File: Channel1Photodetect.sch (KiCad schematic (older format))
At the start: 10 parts

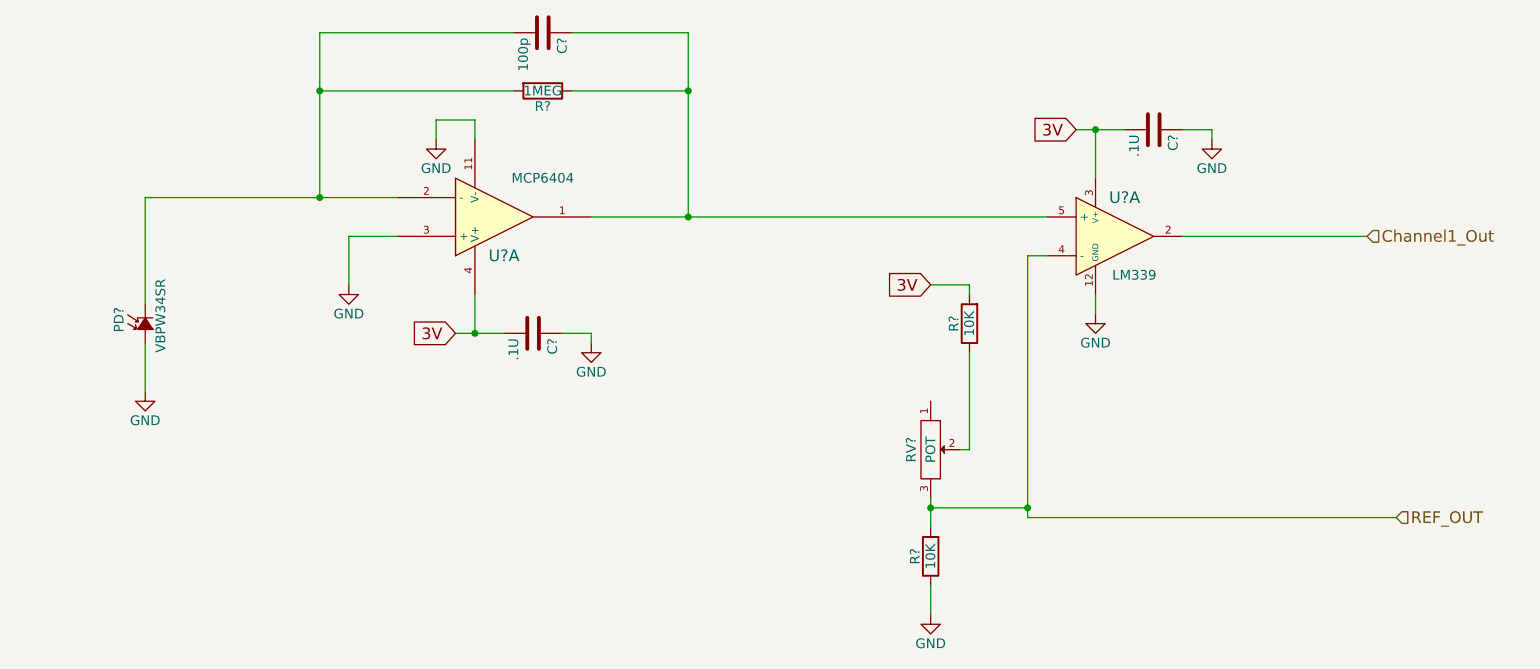
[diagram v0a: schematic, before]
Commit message: Added power regulator, VGND and test points
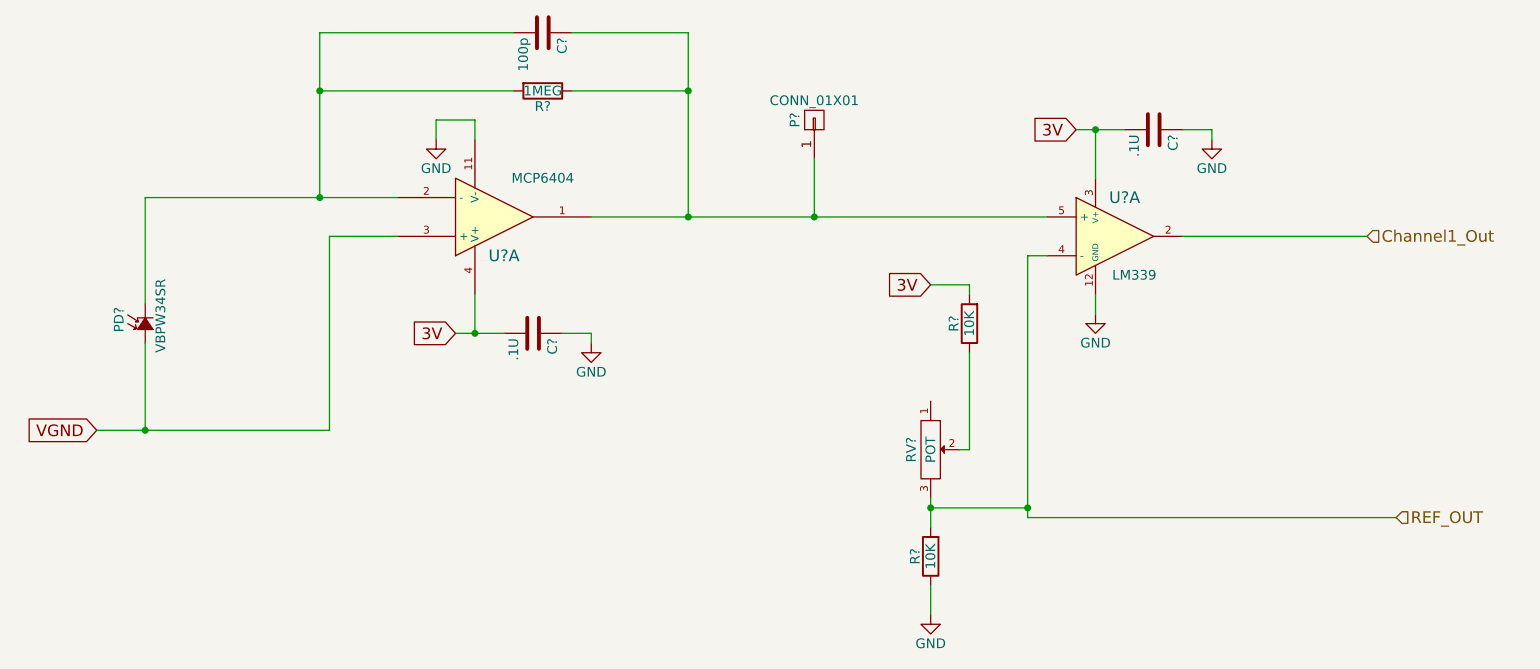
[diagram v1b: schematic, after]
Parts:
- added P?: CONN_01X01, symbol CONN_01X01
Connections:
- net GND: no longer PD?.1 (A), U?.3 (+)
- net at C?.1, R?.1, U?.1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: now also P?.1 (P1)
- new net VGND: PD?.1 (A), U?.3 (+)
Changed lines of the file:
@@
 LIBS:memory
 LIBS:xilinx
-LIBS:special
 LIBS:microcontrollers
 LIBS:dsp
@@
 Wire Wire Line
 	4200 2850 4200 2950
-$Comp
-L GND #PWR?
-U 1 1 5552D532
-P 3750 3700
-F 0 "#PWR?" H 3750 3450 50  0001 C CNN
-F 1 "GND" H 3750 3550 50  0000 C CNN
-F 2 "" H 3750 3700 60  0000 C CNN
-F 3 "" H 3750 3700 60  0000 C CNN
-	1    3750 3700
-	1    0    0    -1
-$EndComp
-Wire Wire Line
-	4000 3450 3750 3450
-Wire Wire Line
-	3750 3450 3750 3700
+Wire Wire Line
+	3650 3450 4000 3450
 Text GLabel 4300 3950 0    60   Input ~ 0
 3V
@@
 Wire Wire Line
 	5000 3950 5000 4000
-$Comp
-L GND #PWR?
-U 1 1 5552D54D
-P 2700 4250
-F 0 "#PWR?" H 2700 4000 50  0001 C CNN
-F 1 "GND" H 2700 4100 50  0000 C CNN
-F 2 "" H 2700 4250 60  0000 C CNN
-F 3 "" H 2700 4250 60  0000 C CNN
-	1    2700 4250
-	1    0    0    -1
-$EndComp
-Wire Wire Line
-	2700 4000 2700 4250
 $Comp
 L LM339 U?
@@
 	7250 4900 9150 4900
 Connection ~ 7250 4850
+$Comp
+L CONN_01X01 P?
+U 1 1 55569411
+P 6150 2850
+F 0 "P?" H 6150 2950 50  0000 C CNN
+F 1 "CONN_01X01" V 6250 2850 50  0000 C CNN
+F 2 "" H 6150 2850 60  0000 C CNN
+F 3 "" H 6150 2850 60  0000 C CNN
+	1    6150 2850
+	0    -1   -1   0
+$EndComp
+Wire Wire Line
+	6150 3050 6150 3350
+Connection ~ 6150 3350
+Wire Wire Line
+	3650 4450 3650 3450
+Wire Wire Line
+	2450 4450 3650 4450
+Wire Wire Line
+	2700 4450 2700 4000
+Text GLabel 2450 4450 0    60   Input ~ 0
+VGND
+Connection ~ 2700 4450
 $EndSCHEMATC

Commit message: Added libraries and imported components into the layout
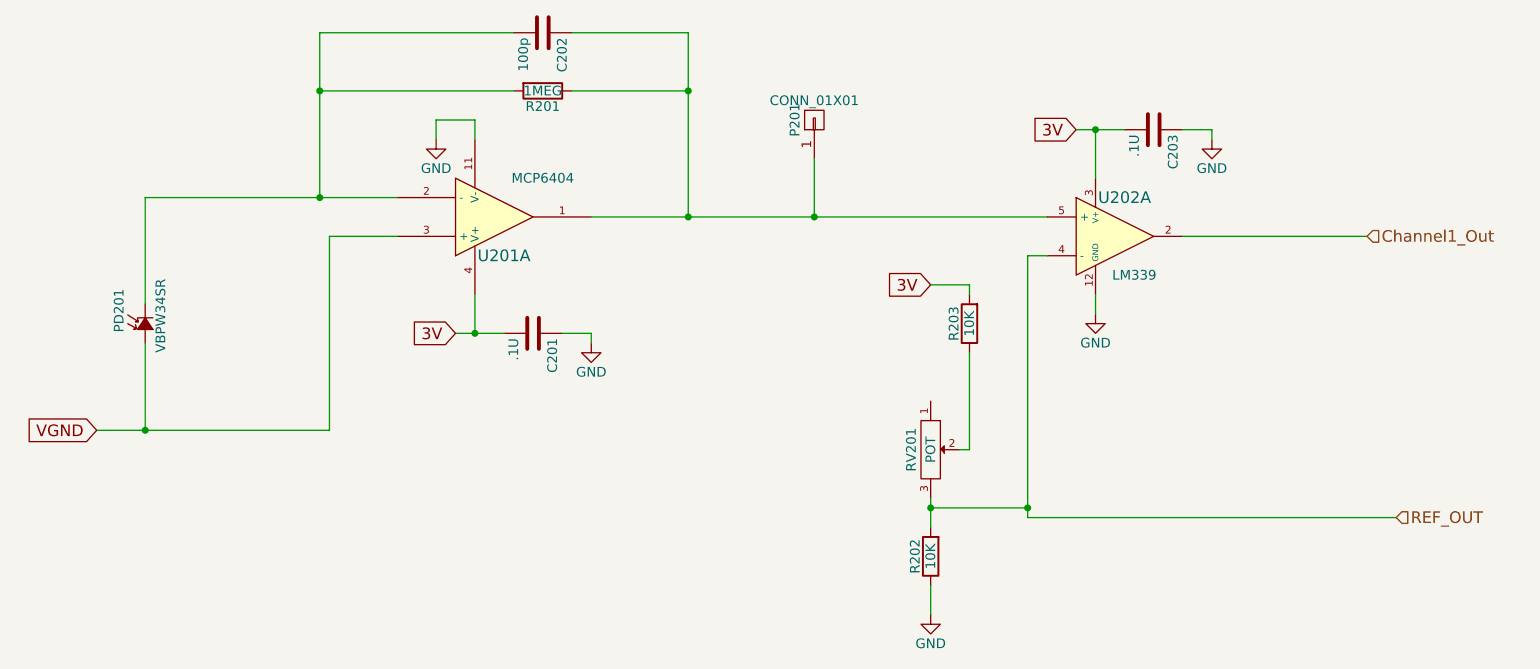
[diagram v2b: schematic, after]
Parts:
- gave numbers to parts that had none: 11
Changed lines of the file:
@@
 $EndDescr
 $Comp
-L R R?
+L R R201
 U 1 1 5552D4FD
 P 4750 2700
-F 0 "R?" V 4830 2700 50  0000 C CNN
+F 0 "R201" V 4830 2700 50  0000 C CNN
 F 1 "1MEG" V 4750 2700 50  0000 C CNN
 F 2 "" V 4680 2700 30  0000 C CNN
@@
 $EndComp
 $Comp
-L C C?
+L C C202
 U 1 1 5552D504
 P 4750 2400
-F 0 "C?" H 4775 2500 50  0000 L CNN
+F 0 "C202" H 4775 2500 50  0000 L CNN
 F 1 "100p" H 4775 2300 50  0000 L CNN
 F 2 "" H 4788 2250 30  0000 C CNN
@@
 $EndComp
 $Comp
-L MCP6404-E/SL U?
+L MCP6404-E/SL U201
 U 1 1 5552D50D
 P 4500 3350
-F 0 "U?" H 4550 3550 60  0000 C CNN
+F 0 "U201" H 4550 3550 60  0000 C CNN
 F 1 "MCP6404" H 4750 3150 50  0000 C CNN
 F 2 "" H 4500 3350 60  0000 C CNN
@@
 $EndComp
 $Comp
-L Photodiode PD?
+L Photodiode PD201
 U 1 1 5552D516
 P 2700 3900
-F 0 "PD?" H 2655 4035 50  0000 L CNN
+F 0 "PD201" H 2655 4035 50  0000 L CNN
 F 1 "VBPW34SR" H 2550 3820 50  0000 L CNN
 F 2 "" V 2700 3900 60  0000 C CNN
@@
 Connection ~ 5500 2700
 $Comp
-L GND #PWR?
+L GND #PWR05
 U 1 1 5552D529
 P 4200 2950
-F 0 "#PWR?" H 4200 2700 50  0001 C CNN
+F 0 "#PWR05" H 4200 2700 50  0001 C CNN
 F 1 "GND" H 4200 2800 50  0000 C CNN
 F 2 "" H 4200 2950 60  0000 C CNN
@@
 	4400 3950 4400 3750
 $Comp
-L C C?
+L C C201
 U 1 1 5552D53D
 P 4700 3950
-F 0 "C?" H 4725 4050 50  0000 L CNN
+F 0 "C201" H 4725 4050 50  0000 L CNN
 F 1 ".1U" H 4725 3850 50  0000 L CNN
 F 2 "" H 4738 3800 30  0000 C CNN
@@
 $EndComp
 $Comp
-L GND #PWR?
+L GND #PWR06
 U 1 1 5552D544
 P 5000 4000
-F 0 "#PWR?" H 5000 3750 50  0001 C CNN
+F 0 "#PWR06" H 5000 3750 50  0001 C CNN
 F 1 "GND" H 5000 3850 50  0000 C CNN
 F 2 "" H 5000 4000 60  0000 C CNN
@@
 	5000 3950 5000 4000
 $Comp
-L LM339 U?
+L LM339 U202
 U 1 1 5552D556
 P 7700 3450
-F 0 "U?" H 7750 3650 60  0000 C CNN
+F 0 "U202" H 7750 3650 60  0000 C CNN
 F 1 "LM339" H 7800 3250 50  0000 C CNN
 F 2 "" H 7700 3450 60  0000 C CNN
@@
 3V
 $Comp
-L R R?
+L R R203
 U 1 1 5552D55F
 P 6950 3900
-F 0 "R?" V 7030 3900 50  0000 C CNN
+F 0 "R203" V 7030 3900 50  0000 C CNN
 F 1 "10K" V 6950 3900 50  0000 C CNN
 F 2 "" V 6880 3900 30  0000 C CNN
@@
 $EndComp
 $Comp
-L R R?
+L R R202
 U 1 1 5552D566
 P 6750 5100
-F 0 "R?" V 6830 5100 50  0000 C CNN
+F 0 "R202" V 6830 5100 50  0000 C CNN
 F 1 "10K" V 6750 5100 50  0000 C CNN
 F 2 "" V 6680 5100 30  0000 C CNN
@@
 $EndComp
 $Comp
-L GND #PWR?
+L GND #PWR07
 U 1 1 5552D56D
 P 6750 5400
-F 0 "#PWR?" H 6750 5150 50  0001 C CNN
+F 0 "#PWR07" H 6750 5150 50  0001 C CNN
 F 1 "GND" H 6750 5250 50  0000 C CNN
 F 2 "" H 6750 5400 60  0000 C CNN
@@
 	6950 3700 6750 3700
 $Comp
-L POT RV?
+L POT RV201
 U 1 1 5552D577
 P 6750 4550
-F 0 "RV?" H 6750 4450 50  0000 C CNN
+F 0 "RV201" H 6750 4450 50  0000 C CNN
 F 1 "POT" H 6750 4550 50  0000 C CNN
 F 2 "" H 6750 4550 60  0000 C CNN
@@
 	7500 2900 7750 2900
 $Comp
-L C C?
+L C C203
 U 1 1 5552D589
 P 7900 2900
-F 0 "C?" H 7925 3000 50  0000 L CNN
+F 0 "C203" H 7925 3000 50  0000 L CNN
 F 1 ".1U" H 7925 2800 50  0000 L CNN
 F 2 "" H 7938 2750 30  0000 C CNN
@@
 $EndComp
 $Comp
-L GND #PWR?
+L GND #PWR08
 U 1 1 5552D590
 P 8200 2950
-F 0 "#PWR?" H 8200 2700 50  0001 C CNN
+F 0 "#PWR08" H 8200 2700 50  0001 C CNN
 F 1 "GND" H 8200 2800 50  0000 C CNN
 F 2 "" H 8200 2950 60  0000 C CNN
@@
 	7600 2900 7600 3150
 $Comp
-L GND #PWR?
+L GND #PWR09
 U 1 1 5552D59A
 P 7600 3850
-F 0 "#PWR?" H 7600 3600 50  0001 C CNN
+F 0 "#PWR09" H 7600 3600 50  0001 C CNN
 F 1 "GND" H 7600 3700 50  0000 C CNN
 F 2 "" H 7600 3850 60  0000 C CNN
@@
 Connection ~ 7250 4850
 $Comp
-L CONN_01X01 P?
+L CONN_01X01 P201
 U 1 1 55569411
 P 6150 2850
-F 0 "P?" H 6150 2950 50  0000 C CNN
+F 0 "P201" H 6150 2950 50  0000 C CNN
 F 1 "CONN_01X01" V 6250 2850 50  0000 C CNN
 F 2 "" H 6150 2850 60  0000 C CNN

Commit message: Added photodiode component to new local footprint library
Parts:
- C201, C202, C203: footprint (none) -> Capacitors_SMD:C_0805_HandSoldering
- P201: footprint (none) -> Pin_Headers:Pin_Header_Straight_1x01
- PD201: footprint (none) -> DasBlinkinput:VPW34SR
- R201: footprint (none) -> Resistors_SMD:R_1206_HandSoldering
- R202, R203: footprint (none) -> Resistors_SMD:R_0805_HandSoldering
- U201, U202: footprint (none) -> Housings_SOIC:SOIC-14_3.9x8.7mm_Pitch1.27mm
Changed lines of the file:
@@
 F 0 "R201" V 4830 2700 50  0000 C CNN
 F 1 "1MEG" V 4750 2700 50  0000 C CNN
-F 2 "" V 4680 2700 30  0000 C CNN
+F 2 "Resistors_SMD:R_1206_HandSoldering" V 4680 2700 30  0001 C CNN
 F 3 "" H 4750 2700 30  0000 C CNN
 F 4 "RC1206FR-071ML" V 4750 2700 60  0001 C CNN "MPN"
@@
 F 0 "C202" H 4775 2500 50  0000 L CNN
 F 1 "100p" H 4775 2300 50  0000 L CNN
-F 2 "" H 4788 2250 30  0000 C CNN
+F 2 "Capacitors_SMD:C_0805_HandSoldering" H 4788 2250 30  0001 C CNN
 F 3 "" H 4750 2400 60  0000 C CNN
 	1    4750 2400
@@
 F 0 "U201" H 4550 3550 60  0000 C CNN
 F 1 "MCP6404" H 4750 3150 50  0000 C CNN
-F 2 "" H 4500 3350 60  0000 C CNN
+F 2 "Housings_SOIC:SOIC-14_3.9x8.7mm_Pitch1.27mm" H 4500 3350 60  0001 C CNN
 F 3 "" H 4500 3350 60  0000 C CNN
 F 4 "MCP6404-E/SL" H 4500 3350 60  0001 C CNN "MPN"
@@
 F 0 "PD201" H 2655 4035 50  0000 L CNN
 F 1 "VBPW34SR" H 2550 3820 50  0000 L CNN
-F 2 "" V 2700 3900 60  0000 C CNN
+F 2 "DasBlinkinput:VPW34SR" V 2700 3900 60  0001 C CNN
 F 3 "" V 2700 3900 60  0000 C CNN
 F 4 "VBPW34SR" H 2700 3900 60  0001 C CNN "MPN"
@@
 F 0 "C201" H 4725 4050 50  0000 L CNN
 F 1 ".1U" H 4725 3850 50  0000 L CNN
-F 2 "" H 4738 3800 30  0000 C CNN
+F 2 "Capacitors_SMD:C_0805_HandSoldering" H 4738 3800 30  0001 C CNN
 F 3 "" H 4700 3950 60  0000 C CNN
 	1    4700 3950
@@
 F 0 "U202" H 7750 3650 60  0000 C CNN
 F 1 "LM339" H 7800 3250 50  0000 C CNN
-F 2 "" H 7700 3450 60  0000 C CNN
+F 2 "Housings_SOIC:SOIC-14_3.9x8.7mm_Pitch1.27mm" H 7700 3450 60  0001 C CNN
 F 3 "" H 7700 3450 60  0000 C CNN
 F 4 "LM339DE4" H 7700 3450 60  0001 C CNN "MPN"
@@
 F 0 "R203" V 7030 3900 50  0000 C CNN
 F 1 "10K" V 6950 3900 50  0000 C CNN
-F 2 "" V 6880 3900 30  0000 C CNN
+F 2 "Resistors_SMD:R_0805_HandSoldering" V 6880 3900 30  0001 C CNN
 F 3 "" H 6950 3900 30  0000 C CNN
 	1    6950 3900
@@
 F 0 "R202" V 6830 5100 50  0000 C CNN
 F 1 "10K" V 6750 5100 50  0000 C CNN
-F 2 "" V 6680 5100 30  0000 C CNN
+F 2 "Resistors_SMD:R_0805_HandSoldering" V 6680 5100 30  0001 C CNN
 F 3 "" H 6750 5100 30  0000 C CNN
 	1    6750 5100
@@
 F 0 "RV201" H 6750 4450 50  0000 C CNN
 F 1 "POT" H 6750 4550 50  0000 C CNN
-F 2 "" H 6750 4550 60  0000 C CNN
+F 2 "" H 6750 4550 60  0001 C CNN
 F 3 "" H 6750 4550 60  0000 C CNN
 F 4 "P090L-02F25BR10K" H 6750 4550 60  0001 C CNN "MPN"
@@
 F 0 "C203" H 7925 3000 50  0000 L CNN
 F 1 ".1U" H 7925 2800 50  0000 L CNN
-F 2 "" H 7938 2750 30  0000 C CNN
+F 2 "Capacitors_SMD:C_0805_HandSoldering" H 7938 2750 30  0001 C CNN
 F 3 "" H 7900 2900 60  0000 C CNN
 	1    7900 2900
@@
 F 0 "P201" H 6150 2950 50  0000 C CNN
 F 1 "CONN_01X01" V 6250 2850 50  0000 C CNN
-F 2 "" H 6150 2850 60  0000 C CNN
+F 2 "Pin_Headers:Pin_Header_Straight_1x01" H 6150 2850 60  0001 C CNN
 F 3 "" H 6150 2850 60  0000 C CNN
 	1    6150 2850

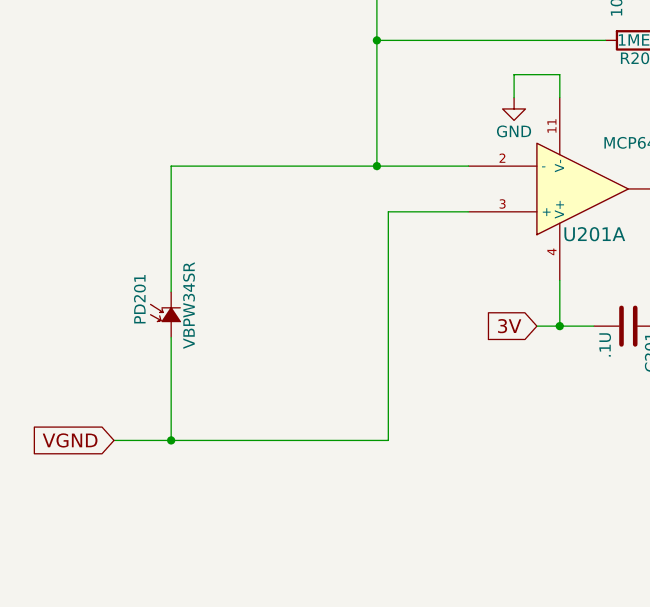
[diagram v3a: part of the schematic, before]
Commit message: Added secondary footprint for photodiode
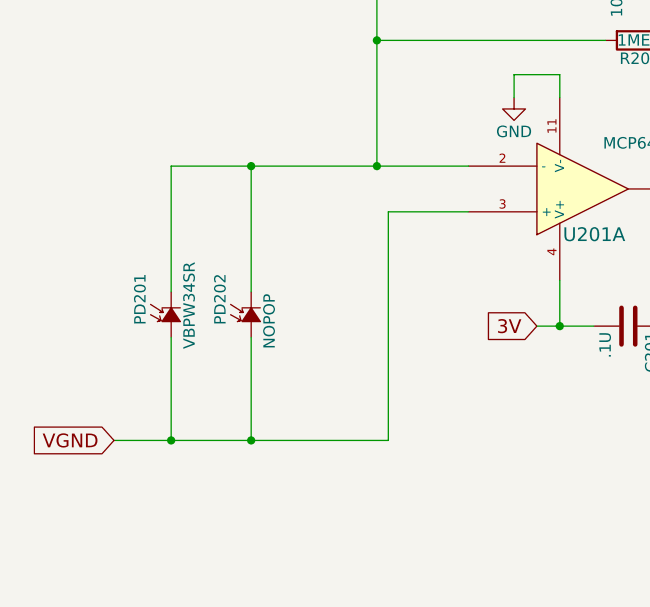
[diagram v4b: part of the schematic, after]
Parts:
- added PD202: NOPOP, Capacitors_SMD:C_0805_HandSoldering, symbol Photodiode
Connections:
- net VGND: now also PD202.1 (A)
- net at C202.2, PD201.2 (C), R201.2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: now also PD202.2 (C)
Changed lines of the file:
@@
 VGND
 Connection ~ 2700 4450
+$Comp
+L Photodiode PD202
+U 1 1 555A3014
+P 3050 3900
+F 0 "PD202" H 3005 4035 50  0000 L CNN
+F 1 "NOPOP" H 2900 3820 50  0000 L CNN
+F 2 "Capacitors_SMD:C_0805_HandSoldering" V 3050 3900 60  0001 C CNN
+F 3 "" V 3050 3900 60  0000 C CNN
+F 4 "TEMD6200FX01" H 3050 3900 60  0001 C CNN "MPN"
+F 5 "http://parts.io/detail/2942502/TEMD6200FX01" H 3050 3900 60  0001 C CNN "Link"
+	1    3050 3900
+	0    -1   -1   0
+$EndComp
+Wire Wire Line
+	3050 3800 3050 3250
+Connection ~ 3050 3250
+Wire Wire Line
+	3050 4000 3050 4450
+Connection ~ 3050 4450
 $EndSCHEMATC

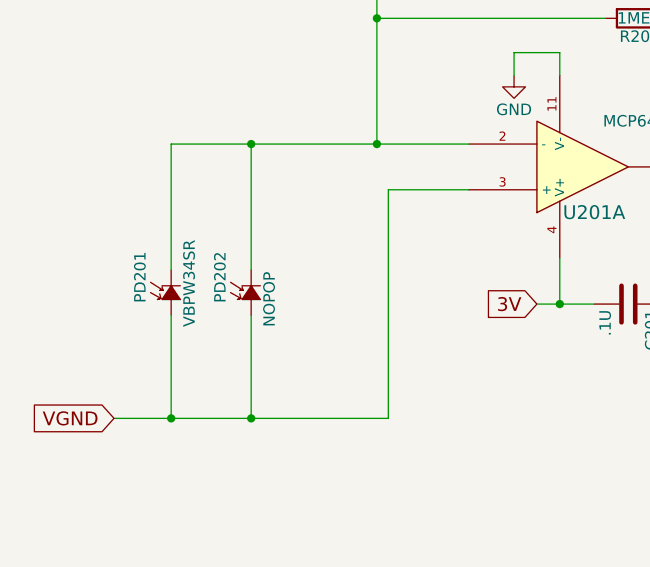
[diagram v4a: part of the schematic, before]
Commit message: Removing extra set of photodiodes and changing the original photodiode footprint
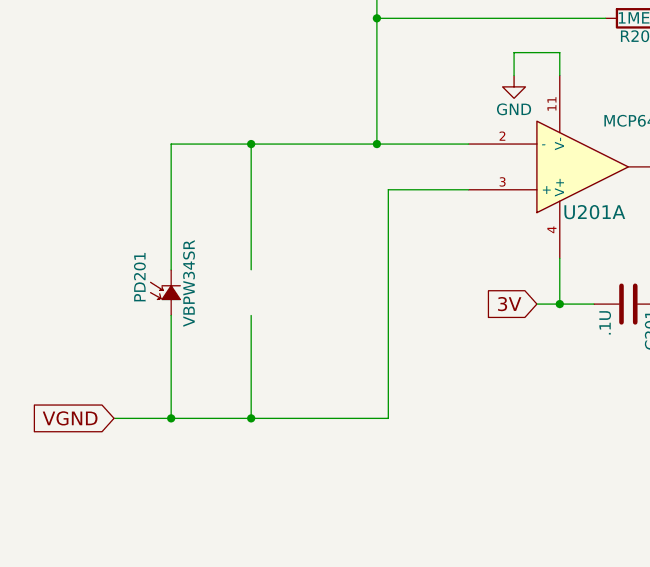
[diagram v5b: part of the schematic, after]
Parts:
- removed PD202: NOPOP, Capacitors_SMD:C_0805_HandSoldering, symbol Photodiode
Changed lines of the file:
@@
 VGND
 Connection ~ 2700 4450
-$Comp
-L Photodiode PD202
-U 1 1 555A3014
-P 3050 3900
-F 0 "PD202" H 3005 4035 50  0000 L CNN
-F 1 "NOPOP" H 2900 3820 50  0000 L CNN
-F 2 "Capacitors_SMD:C_0805_HandSoldering" V 3050 3900 60  0001 C CNN
-F 3 "" V 3050 3900 60  0000 C CNN
-F 4 "TEMD6200FX01" H 3050 3900 60  0001 C CNN "MPN"
-F 5 "http://parts.io/detail/2942502/TEMD6200FX01" H 3050 3900 60  0001 C CNN "Link"
-	1    3050 3900
-	0    -1   -1   0
-$EndComp
 Wire Wire Line
 	3050 3800 3050 3250
